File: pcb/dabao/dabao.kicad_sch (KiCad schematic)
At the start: 65 parts, among them J1 Conn_01x05, J2 USB_C_Receptacle_USB2.0_16P, J3 Conn_01x04, J4 Conn_01x04_Pin, J5 Conn_Battery, J6 Conn_01x04, J7 Conn_01x04, J8 Display, SW1 SW_RESET, SW2 SW_POWER, U1 nice_nano, U2 MCP23017_SP

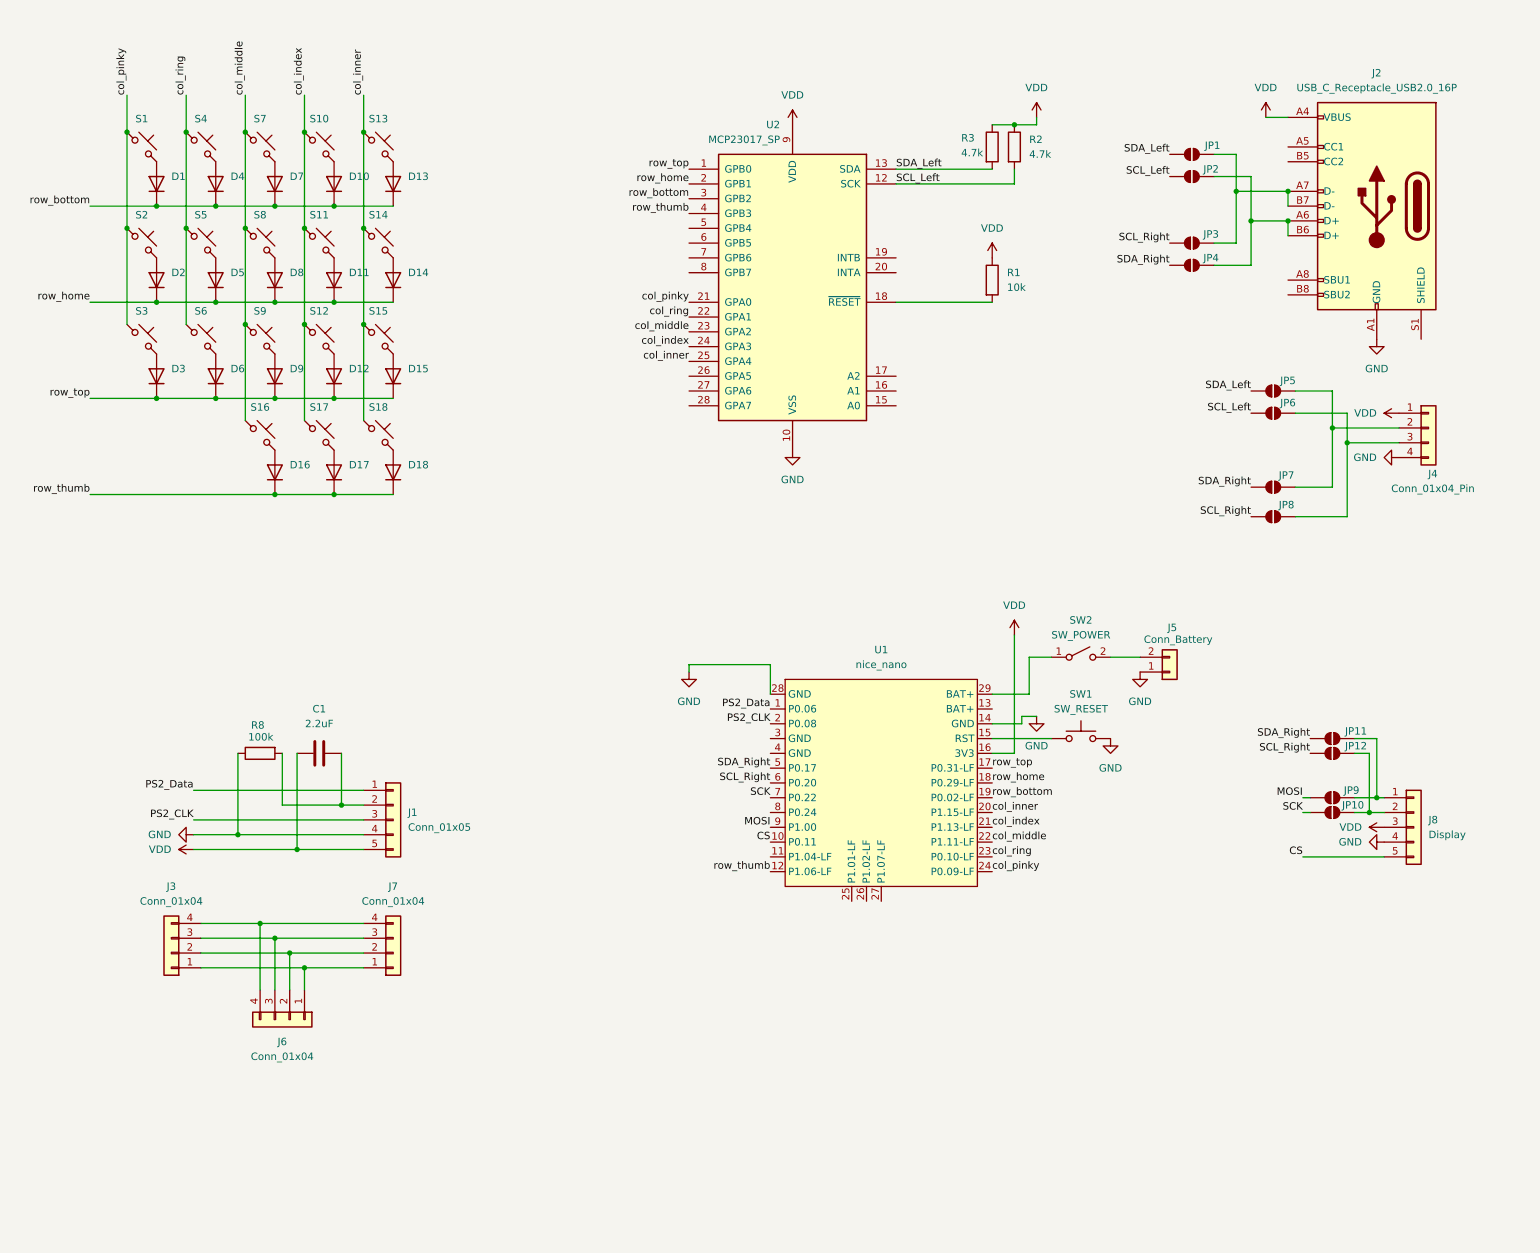
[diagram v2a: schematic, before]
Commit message: Clean up schematic
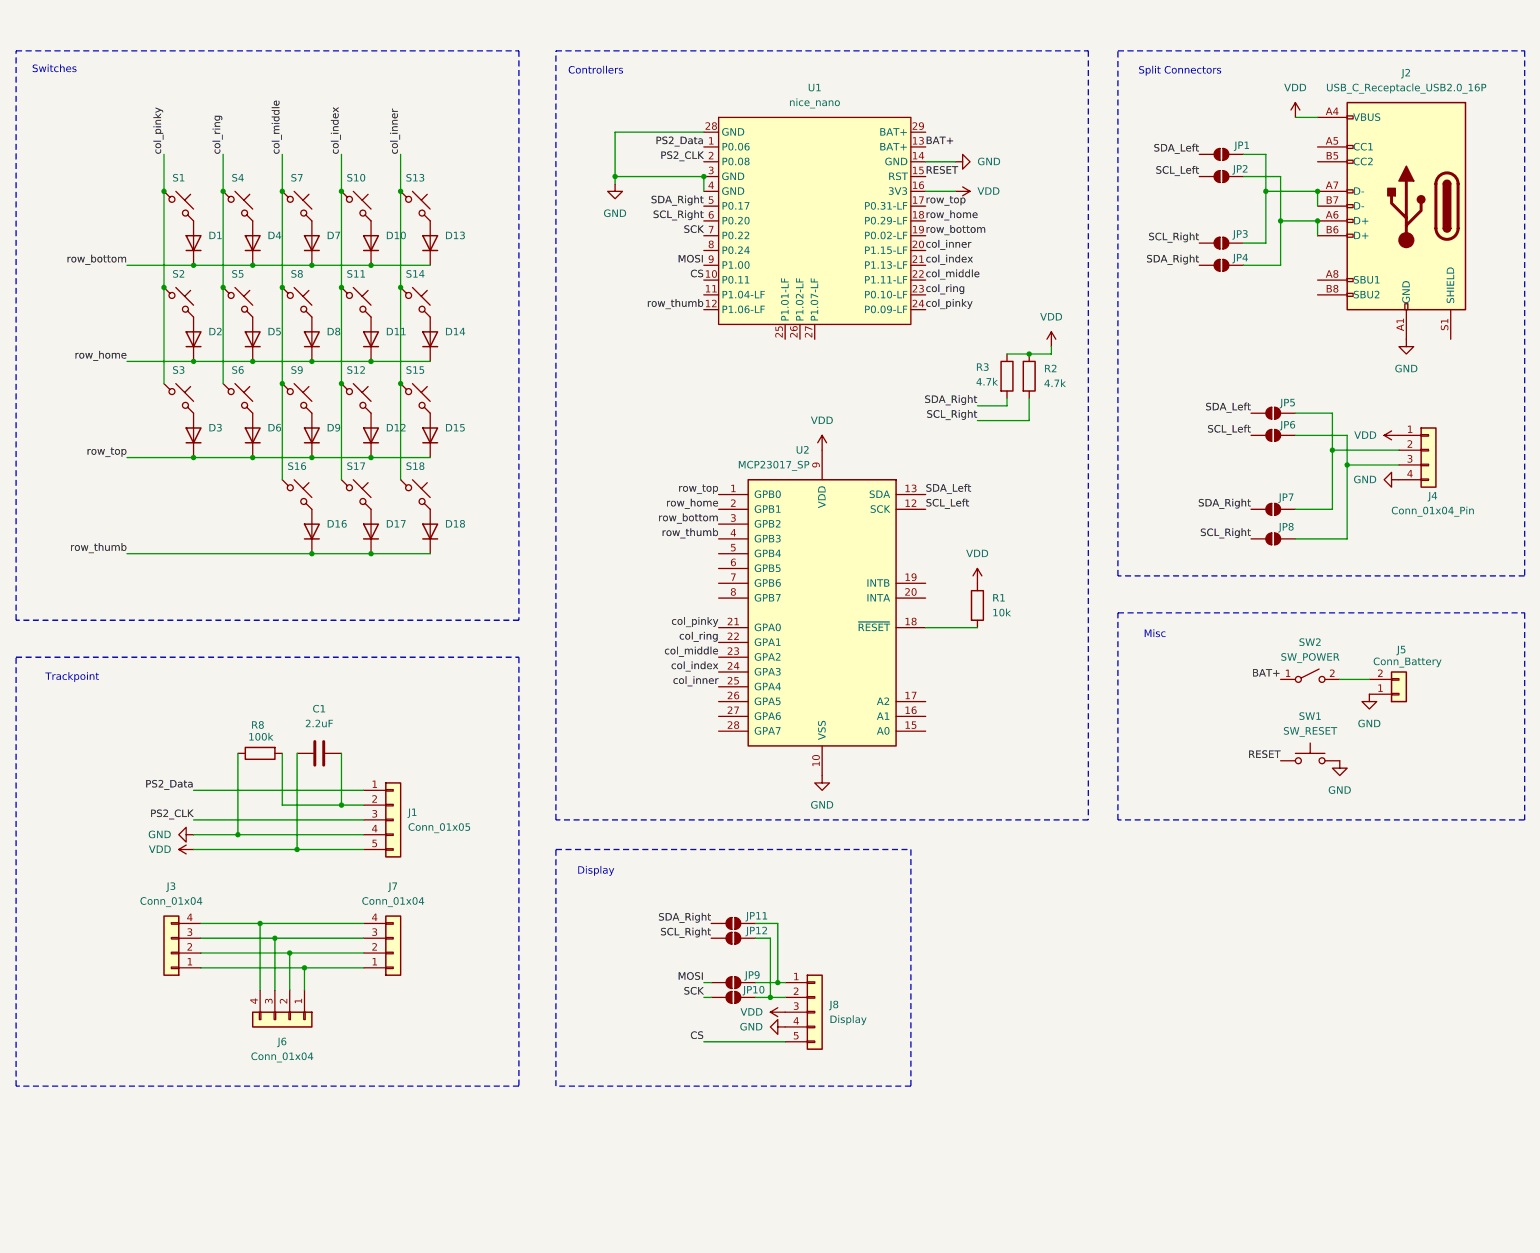
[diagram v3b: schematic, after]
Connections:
- net GND: now also U1.3 (GND), U1.4 (GND)
- net SCL_Left: no longer R2.2
- net SCL_Right: now also R2.2
- net SDA_Left: no longer R3.2
- net SDA_Right: now also R3.2
- net RESET: now reaches SW1.1, U1.15 (RST)
- net BAT+: now reaches U1.13 (BAT+)
- net BAT+: now also SW2.1 (A)
- net at U1.29 (BAT+): no longer SW2.1 (A)
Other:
- note added: "Controllers"
- note added: "Display"
- note added: "Misc"
- note added: "Split Connectors"
- note added: "Switches"
- note added: "Trackpoint"
- moved on the sheet: D1, D10, D11, D12, D13, D14, D15, D16, D17, D18, D2, D3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

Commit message: Fix connectors in layout, add board outline, start routing
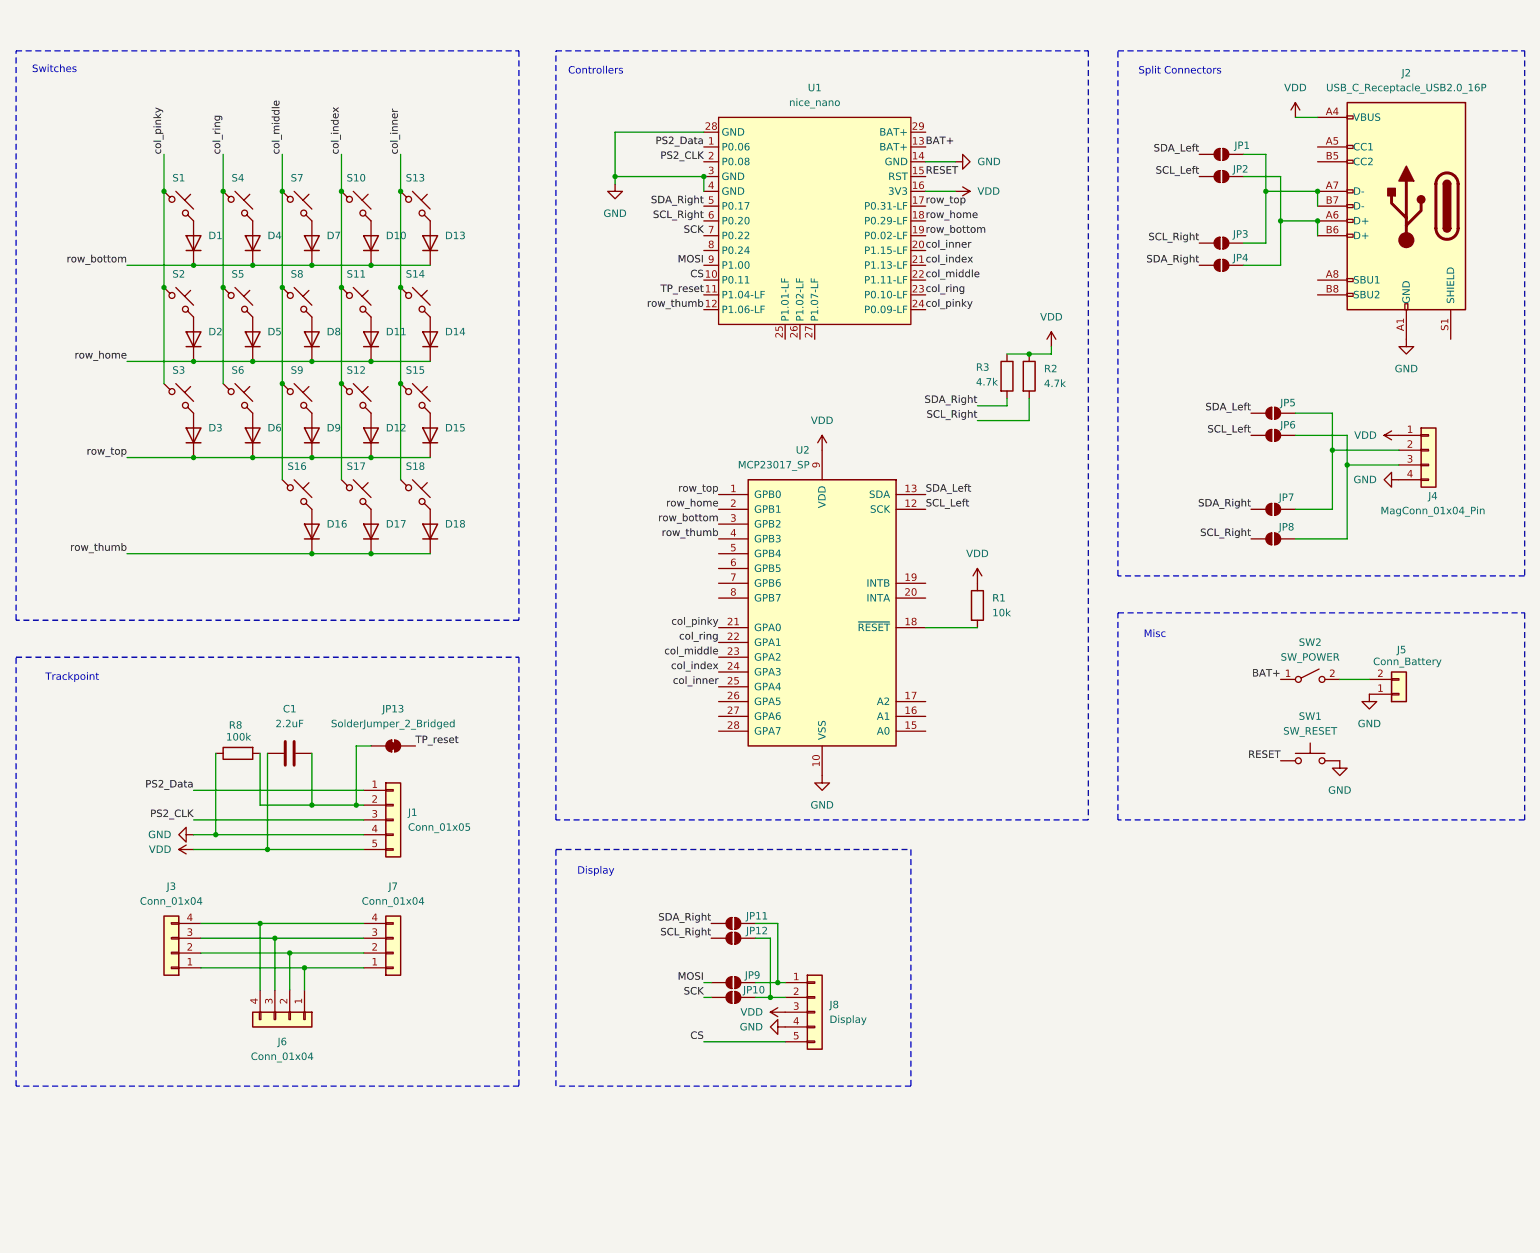
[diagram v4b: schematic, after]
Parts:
- added JP13: SolderJumper_2_Bridged, Jumper:SolderJumper-2_P1.3mm_Bridged_Pad1.0x1.5mm, symbol Jumper:SolderJumper_2_Bridged
- J4: value Conn_01x04_Pin -> MagConn_01x04_Pin
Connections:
- net TP_reset: now reaches U1.11 (P1.04-LF)
- net TP_reset: now also JP13.2 (B)
- net at C1.2, J1.2 (Pin_2), R8.2: now also JP13.1 (A)
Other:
- moved on the sheet: C1, R8
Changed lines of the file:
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@@
 	)
 	(junction
-		(at 57.15 149.86)
-		(diameter 0)
-		(color 0 0 0 0)
-	)
-	(junction
 		(at 69.85 52.07)
 		(diameter 0)
@@
 	)
 	(junction
-		(at 67.31 152.4)
-		(diameter 0)
-		(color 0 0 0 0)
-	)
-	(junction
 		(at 148.59 177.8)
 		(diameter 0)
@@
 	)
 	(junction
+		(at 77.47 144.78)
+		(diameter 0)
+		(color 0 0 0 0)
+	)
+	(junction
 		(at 74.93 72.39)
 		(diameter 0)
@@
 	)
 	(junction
-		(at 68.58 172.72)
+		(at 53.34 149.86)
 		(diameter 0)
 		(color 0 0 0 0)
 	)
 	(junction
-		(at 85.09 55.88)
+		(at 68.58 172.72)
 		(diameter 0)
 		(color 0 0 0 0)
 	)
 	(junction
-		(at 247.65 86.36)
+		(at 85.09 55.88)
 		(diameter 0)
 		(color 0 0 0 0)
 	)
 	(junction
-		(at 74.93 144.78)
+		(at 247.65 86.36)
 		(diameter 0)
 		(color 0 0 0 0)
@@
 	)
 	(junction
+		(at 62.23 152.4)
+		(diameter 0)
+		(color 0 0 0 0)
+	)
+	(junction
 		(at 59.69 52.07)
 		(diameter 0)
@@
 	)
 	(junction
+		(at 69.85 144.78)
+		(diameter 0)
+		(color 0 0 0 0)
+	)
+	(junction
 		(at 59.69 85.09)
 		(diameter 0)
@@
 	(wire
 		(pts
+			(xy 69.85 144.78) (xy 77.47 144.78)
+		)
+		(stroke
+			(width 0)
+			(type default)
+		)
+	)
+	(wire
+		(pts
 			(xy 238.76 93.98) (xy 245.11 93.98)
 		)
@@
 	(wire
 		(pts
-			(xy 49.53 149.86) (xy 57.15 149.86)
+			(xy 49.53 149.86) (xy 53.34 149.86)
 		)
 		(stroke
@@
 	(wire
 		(pts
-			(xy 49.53 152.4) (xy 67.31 152.4)
+			(xy 49.53 152.4) (xy 62.23 152.4)
 		)
 		(stroke
@@
 	(wire
 		(pts
+			(xy 62.23 152.4) (xy 78.74 152.4)
+		)
+		(stroke
+			(width 0)
+			(type default)
+		)
+	)
+	(wire
+		(pts
 			(xy 50.8 172.72) (xy 68.58 172.72)
 		)
@@
 	(wire
 		(pts
-			(xy 74.93 135.89) (xy 74.93 144.78)
+			(xy 69.85 135.89) (xy 69.85 144.78)
 		)
 		(stroke
@@
 	(wire
 		(pts
-			(xy 57.15 149.86) (xy 78.74 149.86)
-		)
-		(stroke
-			(width 0)
-			(type default)
-		)
-	)
-	(wire
-		(pts
 			(xy 80.01 101.6) (xy 90.17 101.6)
 		)
@@
 	(wire
 		(pts
-			(xy 64.77 144.78) (xy 74.93 144.78)
+			(xy 60.96 144.78) (xy 69.85 144.78)
 		)
 		(stroke
@@
 	(wire
 		(pts
-			(xy 74.93 144.78) (xy 78.74 144.78)
+			(xy 64.77 39.37) (xy 64.77 55.88)
 		)
 		(stroke
@@
 	(wire
 		(pts
-			(xy 64.77 39.37) (xy 64.77 55.88)
+			(xy 80.01 134.62) (xy 77.47 134.62)
 		)
 		(stroke
@@
 	(wire
 		(pts
-			(xy 57.15 135.89) (xy 57.15 149.86)
+			(xy 53.34 135.89) (xy 53.34 149.86)
 		)
 		(stroke
@@
 	(wire
 		(pts
+			(xy 53.34 149.86) (xy 78.74 149.86)
+		)
+		(stroke
+			(width 0)
+			(type default)
+		)
+	)
+	(wire
+		(pts
 			(xy 146.05 165.1) (xy 149.86 165.1)
 		)
@@
 	(wire
 		(pts
+			(xy 77.47 144.78) (xy 78.74 144.78)
+		)
+		(stroke
+			(width 0)
+			(type default)
+		)
+	)
+	(wire
+		(pts
 			(xy 189.23 67.31) (xy 193.04 67.31)
 		)
@@
 	(wire
 		(pts
-			(xy 64.77 135.89) (xy 64.77 144.78)
+			(xy 60.96 135.89) (xy 60.96 144.78)
 		)
 		(stroke
@@
 	(wire
 		(pts
-			(xy 67.31 135.89) (xy 67.31 152.4)
+			(xy 62.23 135.89) (xy 62.23 152.4)
 		)
 		(stroke
@@
 	(wire
 		(pts
-			(xy 246.38 123.19) (xy 251.46 123.19)
+			(xy 77.47 134.62) (xy 77.47 144.78)
 		)
 		(stroke
@@
 	(wire
 		(pts
-			(xy 189.23 76.2) (xy 189.23 74.93)
+			(xy 246.38 123.19) (xy 251.46 123.19)
 		)
 		(stroke
@@
 	(wire
 		(pts
-			(xy 38.1 101.6) (xy 69.85 101.6)
+			(xy 189.23 76.2) (xy 189.23 74.93)
 		)
 		(stroke
@@
 	(wire
 		(pts
-			(xy 66.04 170.18) (xy 66.04 176.53)
+			(xy 38.1 101.6) (xy 69.85 101.6)
 		)
 		(stroke
@@
 	(wire
 		(pts
-			(xy 67.31 152.4) (xy 78.74 152.4)
+			(xy 66.04 170.18) (xy 66.04 176.53)
 		)
 		(stroke
@@
 		)
 	)
+	(label "TP_reset"
+		(at 87.63 134.62 0)
+		(effects
+			(font
+				(size 1.27 1.27)
+			)
+			(justify left bottom)
+		)
+	)
 	(label "PS2_Data"
 		(at 137.16 31.75 180)
@@
 		)
 	)
+	(label "TP_reset"
+		(at 137.16 57.15 180)
+		(effects
+			(font
+				(size 1.27 1.27)
+			)
+			(justify right bottom)
+		)
+	)
 	(label "row_home"
 		(at 175.26 44.45 0)
@@
 	)
 	(symbol
+		(lib_id "Jumper:SolderJumper_2_Bridged")
+		(at 83.82 134.62 0)
+		(unit 1)
+		(exclude_from_sim no)
+		(in_bom no)
+		(on_board yes)
+		(dnp no)
+		(fields_autoplaced yes)
+		(property "Reference" "JP13"
+			(at 83.82 128.27 0)
+			(effects
+				(font
+					(size 1.27 1.27)
+				)
+			)
+		)
+		(property "Value" "SolderJumper_2_Bridged"
+			(at 83.82 130.81 0)
+			(effects
+				(font
+					(size 1.27 1.27)
+				)
+			)
+		)
+		(property "Footprint" "Jumper:SolderJumper-2_P1.3mm_Bridged_Pad1.0x1.5mm"
+			(at 83.82 134.62 0)
+			(effects
+				(font
+					(size 1.27 1.27)
+				)
+				(hide yes)
+			)
+		)
+		(property "Datasheet" "~"
+			(at 83.82 134.62 0)
+			(effects
+				(font
+					(size 1.27 1.27)
+				)
+				(hide yes)
+			)
+		)
+		(property "Description" "Solder Jumper, 2-pole, closed/bridged"
+			(at 83.82 134.62 0)
+			(effects
+				(font
+					(size 1.27 1.27)
+				)
+				(hide yes)
+			)
+		)
+		(pin "1"
+		)
+		(pin "2"
+		)
+		(instances
+			(project ""
+				(path "/f7dfc45c-83ad-43c7-9815-463af0b28fbd"
+					(reference "JP13")
+					(unit 1)
+				)
+			)
+		)
+	)
+	(symbol
 		(lib_id "power:GND")
 		(at 180.34 34.29 90)
@@
 	(symbol
 		(lib_id "Device:R")
-		(at 60.96 135.89 90)
+		(at 57.15 135.89 90)
 		(mirror x)
 		(unit 1)
@@
 		(dnp no)
 		(property "Reference" "R8"
-			(at 61.722 131.064 90)
+			(at 57.912 131.064 90)
 			(effects
 				(font
@@
 		)
 		(property "Value" "100k"
-			(at 63.246 133.096 90)
+			(at 59.436 133.096 90)
 			(effects
 				(font
@@
 		)
 		(property "Footprint" "Resistor_SMD:R_0805_2012Metric"
-			(at 60.96 134.112 90)
+			(at 57.15 134.112 90)
 			(effects
 				(font
@@
 		)
 		(property "Datasheet" "~"
-			(at 60.96 135.89 0)
+			(at 57.15 135.89 0)
 			(effects
 				(font
@@
 		)
 		(property "Description" "Resistor"
-			(at 60.96 135.89 0)
+			(at 57.15 135.89 0)
 			(effects
 				(font
@@
 			)
 		)
-		(property "Value" "Conn_01x04_Pin"
+		(property "Value" "MagConn_01x04_Pin"
 			(at 262.382 94.234 0)
 			(effects
@@
 	(symbol
 		(lib_id "Device:C")
-		(at 71.12 135.89 90)
+		(at 66.04 135.89 90)
 		(unit 1)
 		(exclude_from_sim no)
@@
 		(fields_autoplaced yes)
 		(property "Reference" "C1"
-			(at 71.12 128.27 90)
+			(at 66.04 128.27 90)
 			(effects
 				(font
@@
 		)
 		(property "Value" "2.2uF"
-			(at 71.12 130.81 90)
+			(at 66.04 130.81 90)
 			(effects
 				(font
@@
 		)
 		(property "Footprint" "Capacitor_SMD:C_0805_2012Metric"
-			(at 74.93 134.9248 0)
+			(at 69.85 134.9248 0)
 			(effects
 				(font
@@
 		)
 		(property "Datasheet" "~"
-			(at 71.12 135.89 0)
+			(at 66.04 135.89 0)
 			(effects
 				(font
@@
 		)
 		(property "Description" "Unpolarized capacitor"
-			(at 71.12 135.89 0)
+			(at 66.04 135.89 0)
 			(effects
 				(font

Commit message: Add missing pullups on ps2 lines
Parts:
- added R4, R5: 4.7k, Resistor_SMD:R_0805_2012Metric, symbol Device:R
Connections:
- net PS2_CLK: now also R4.1
- net PS2_Data: now also R5.1
- net VDD: now also R4.2, R5.2
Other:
- moved on the sheet: C1, R8
